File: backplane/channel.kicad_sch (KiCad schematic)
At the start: 14 parts, among them U5 mini-560, Y2 Crystal_GND24

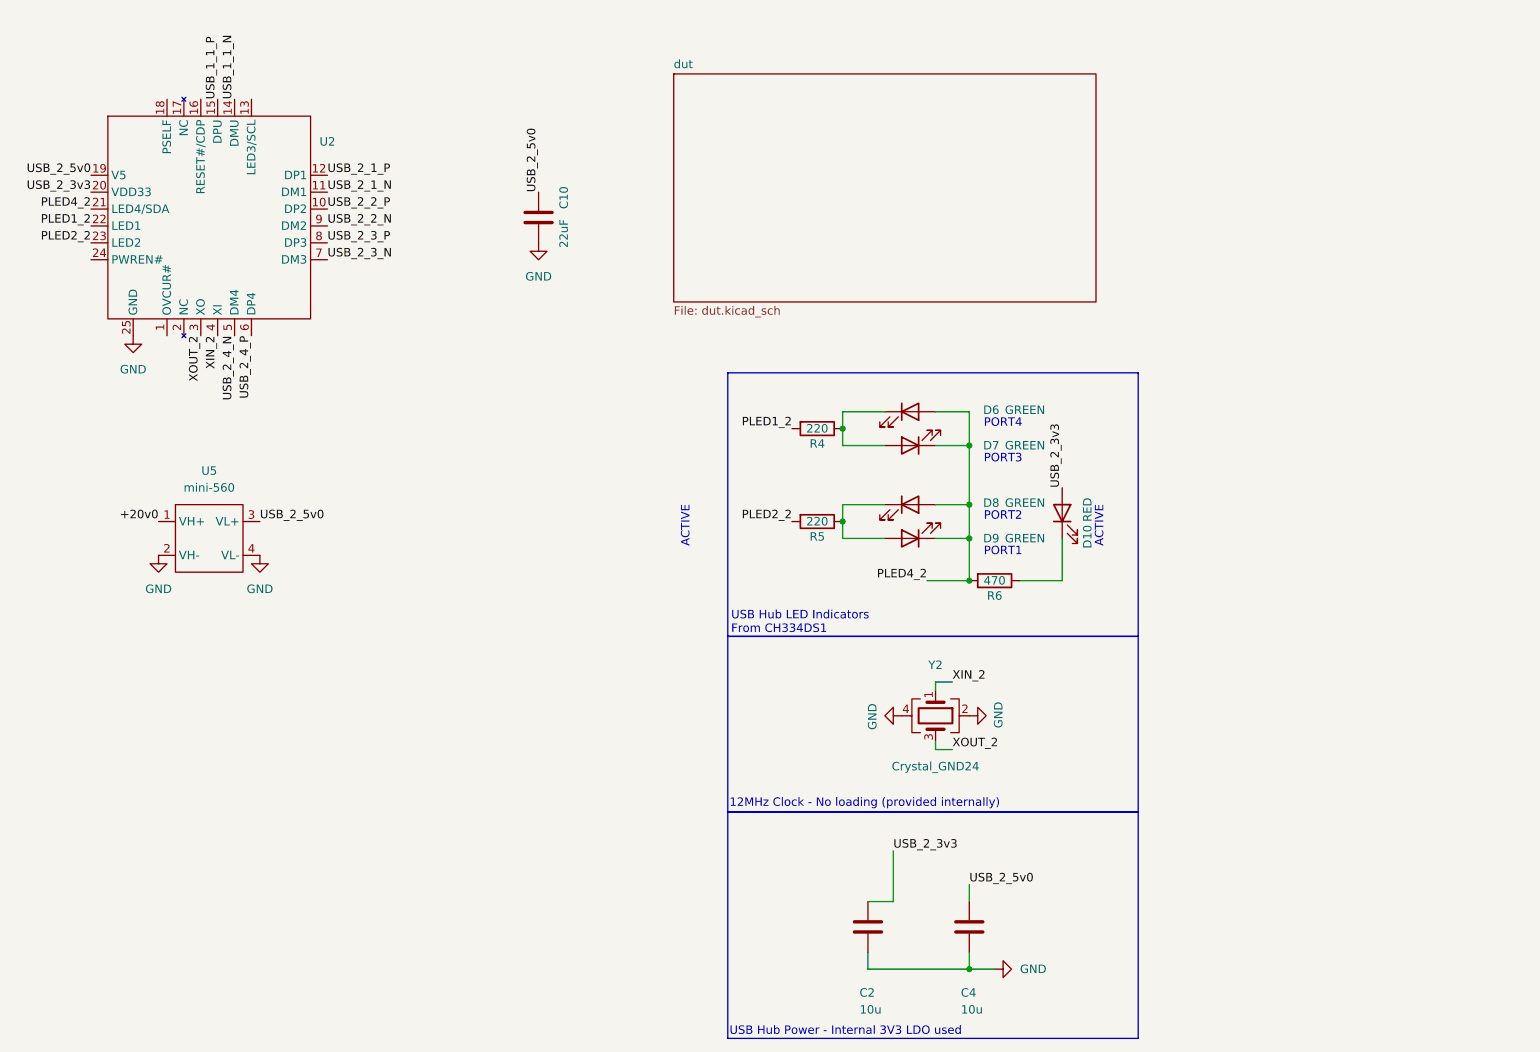
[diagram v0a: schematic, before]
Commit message: Add 20V -> 3V3 buck
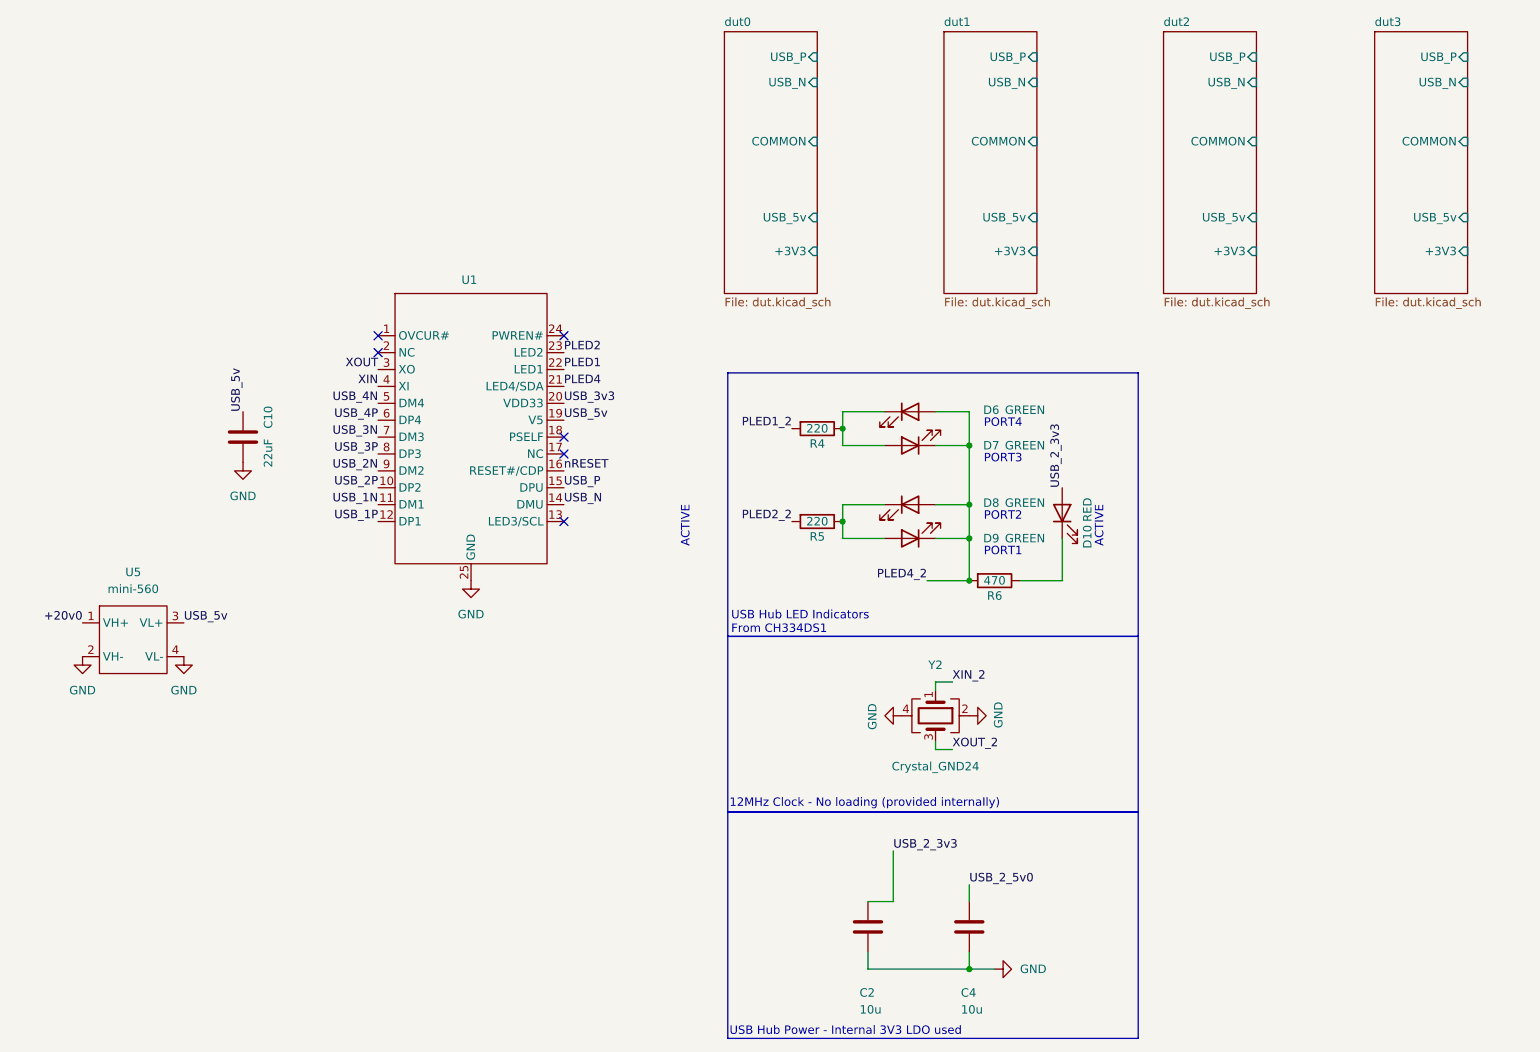
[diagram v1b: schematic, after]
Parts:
- removed U2: ~, Package_DFN_QFN:QFN-24-1EP_4x4mm_P0.5mm_EP2.7x2.7mm_ThermalVias, symbol backbone-16:CH334F
- added U1: ~, Package_DFN_QFN:QFN-24-1EP_4x4mm_P0.5mm_EP2.7x2.7mm_ThermalVias, symbol hive:CH334F
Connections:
- net GND: now also U1.25 (GND)
- net USB_2_5v0: no longer C10.1, U5.3 (VL+)
- new net PLED1: U1.22 (LED1)
- new net PLED2: U1.23 (LED2)
- new net PLED4: U1.21 (LED4/SDA)
- new net USB_1N: U1.11 (DM1)
- new net USB_1P: U1.12 (DP1)
- new net USB_2N: U1.9 (DM2)
- new net USB_2P: U1.10 (DP2)
- new net USB_3N: U1.7 (DM3)
- new net USB_3P: U1.8 (DP3)
- new net USB_3v3: U1.20 (VDD33)
- new net USB_4N: U1.5 (DM4)
- new net USB_4P: U1.6 (DP4)
- new net USB_5v: C10.1, U1.19 (V5), U5.3 (VL+)
- new net USB_N: U1.14 (DMU)
- new net USB_P: U1.15 (DPU)
- new net XIN: U1.4 (XI)
- new net XOUT: U1.3 (XO)
- new net nRESET: U1.16 (RESET#/CDP)
- no-connect marks 0 -> 6
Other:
- sheet dut renamed dut0
- added sheet dut1 (dut.kicad_sch)
- added sheet dut2 (dut.kicad_sch)
- added sheet dut3 (dut.kicad_sch)
- sheet dut0 ports: added +3V3, COMMON, USB_5v, USB_N, USB_P; removed none
- moved on the sheet: C10, U5

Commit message: More work on the backplane
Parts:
- renumbered C4 to C10, C10 to C8, C2 to C9, D8 to D10, D9 to D11, D10 to D12, D6 to D8, D7 to D9, R4 to R13, R5 to R14, R6 to R15, U5 to U4, U1 to U5
